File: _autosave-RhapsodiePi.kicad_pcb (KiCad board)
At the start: 6 copper layers, 85.2 x 56.1 mm, 261 parts, among them J1 Micro_SD_Card_Det, J2 Conn_Coaxial, J3 Conn_02x05_Odd_Even, J4 USB_A_Stacked, J5 USB_A_Stacked, J7 RJ45_HR913550A, J8 HDMI_A, J9 AudioJack4, P1 USB_C_Plug, U1 IMX6UL, U10 FE2.1, U11 RTL8201F, U12 TFP410PAP, U13 LM4871, U14 LM4871, U15 TPS65185RGZR, U2 MT3420C-mt3420c, U3 MT3420C-mt3420c, U4 MT3420C-mt3420c, U5 MKDN0xxxCL, U6 MT41K256M16TW, U7 MT41K256M16TW, U8 X1000, U9 AP6212, Y1 12MHz, Y2 24MHz, Y3 32.768kHz

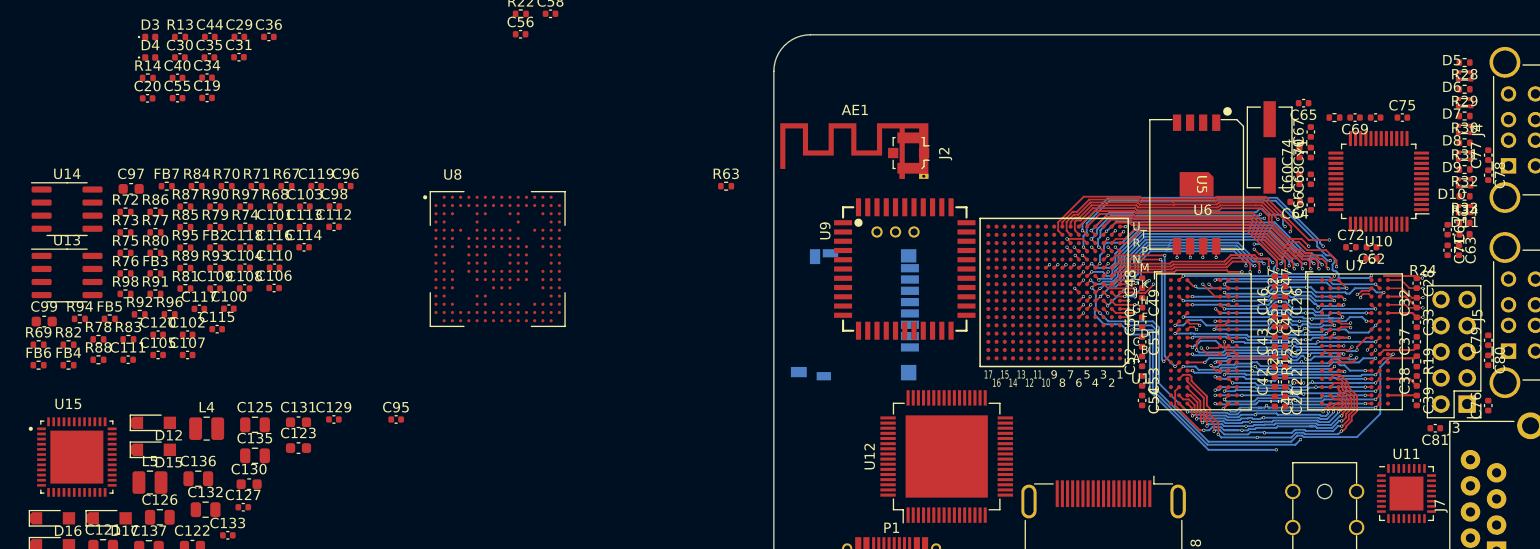
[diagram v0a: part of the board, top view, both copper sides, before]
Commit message: update DDR
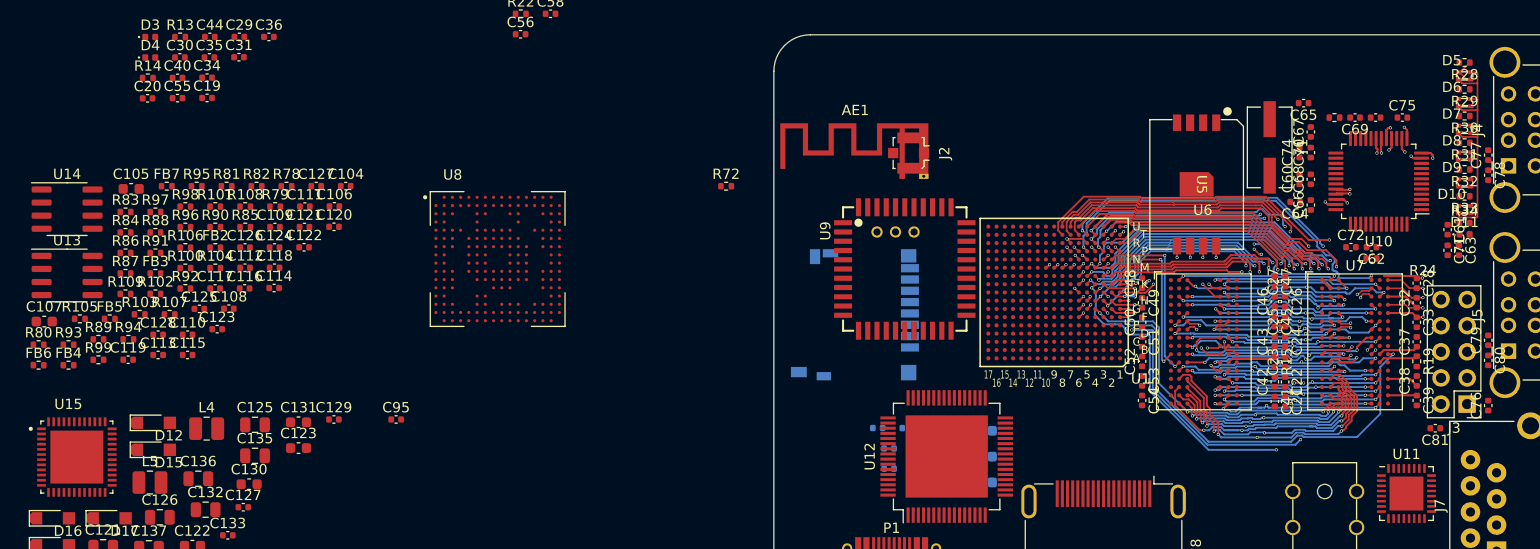
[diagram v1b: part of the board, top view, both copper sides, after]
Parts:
- added C100: 22µ, Capacitor_SMD:C_0603_1608Metric, B.Cu at (104.8, 107.9)
- added C101: 100n, Capacitor_SMD:C_0402_1005Metric, B.Cu at (95.5, 106.5)
- added C102: 100n, Capacitor_SMD:C_0402_1005Metric, B.Cu at (94.4, 102.6)
- added C103: 100n, Capacitor_SMD:C_0402_1005Metric, B.Cu at (98.4, 107.1)
- added C96: 22µ, Capacitor_SMD:C_0603_1608Metric, B.Cu at (104.8, 102.8)
- added C97: 100n, Capacitor_SMD:C_0402_1005Metric, B.Cu at (95.5, 104.6)
- added C98: 22µ, Capacitor_SMD:C_0603_1608Metric, B.Cu at (104.8, 105.4)
- added C99: 22µ, Capacitor_SMD:C_0603_1608Metric, B.Cu at (100.8, 102.8)
- added R62: 330, Resistor_SMD:R_0402_1005Metric, B.Cu at (97.3, 102.6)
- added R63: 330, Resistor_SMD:R_0402_1005Metric, B.Cu at (101.3, 105.1)
- added R67: 330, Resistor_SMD:R_0402_1005Metric, B.Cu at (98.4, 105.1)
- added R71: 2K7, Resistor_SMD:R_0402_1005Metric, B.Cu at (101.3, 107.1)
- renumbered C96 to C104, C97 to C105, C98 to C106, C99 to C107, C100 to C108, C101 to C109, C102 to C110, C103 to C111, C104 to C112, C105 to C113, C106 to C114, C107 to C115, C108 to C116, C109 to C117, C110 to C118, C111 to C119, C112 to C120, C113 to C121, C114 to C122, C115 to C123, C116 to C124, C117 to C125, C118 to C126, C119 to C127, C120 to C128, R89 to R100, R90 to R101, R91 to R102, R92 to R103, R93 to R104, R94 to R105, R95 to R106, R96 to R107, R97 to R108, R98 to R109, R63 to R72, R67 to R78, R68 to R79, R69 to R80, R70 to R81, R71 to R82, R72 to R83, R73 to R84, R74 to R85, R75 to R86, R76 to R87, R77 to R88, R78 to R89, R79 to R90, R80 to R91, R81 to R92, R82 to R93, R83 to R94, R84 to R95, R85 to R96, R86 to R97, R87 to R98, R88 to R99
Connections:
- net Net-(J4-Pad2) renamed /USB/D1-
- net Net-(J4-Pad3) renamed /USB/D1+
- net Net-(J4-Pad6) renamed /USB/D2-
- net Net-(J4-Pad7) renamed /USB/D2+
- net Net-(J5-Pad2) renamed /USB/D3-
- net Net-(J5-Pad3) renamed /USB/D3+
- net Net-(J5-Pad6) renamed /USB/D4-
- net Net-(J5-Pad7) renamed /USB/D4+
- AE1 pad 2: AGND2 -> GND
- C1 pad 2: AGND2 -> GND
- C10 pad 1: AGND2 -> GND
- C104 pad 1: AGND2 -> GND
- C105 pad 1: AGND2 -> GND
- C106 pad 1: AGND2 -> GND
- C107 pad 1: AGND2 -> GND
- C108 pad 2: AGND2 -> GND
- C11 pad 2: AGND2 -> GND
- C119 pad 1: AGND2 -> GND
- C12 pad 1: AGND2 -> GND
- C121 pad 2: AGND2 -> GND
- C122 pad 1: AGND2 -> GND
- C124 pad 2: AGND2 -> GND
- C125 pad 1: AGND2 -> GND
- C126 pad 1: AGND2 -> GND
- C127 pad 1: Net-(C119-Pad1) -> Net-(C127-Pad1)
- C127 pad 2: AGND2 -> GND
- C128 pad 1: Net-(C120-Pad1) -> Net-(C128-Pad1)
- C128 pad 2: AGND2 -> GND
- C13 pad 2: AGND2 -> GND
- C14 pad 1: AGND2 -> GND
- C15 pad 1: AGND2 -> GND
- C16 pad 1: AGND2 -> GND
- C17 pad 2: AGND2 -> GND
- C18 pad 1: AGND2 -> GND
- C19 pad 2: AGND2 -> GND
- C2 pad 2: AGND2 -> GND
- C20 pad 2: AGND2 -> GND
- C21 pad 2: AGND2 -> GND
- C22 pad 2: AGND2 -> GND
- C23 pad 2: AGND2 -> GND
- C24 pad 2: AGND2 -> GND
- C25 pad 2: AGND2 -> GND
- C26 pad 2: AGND2 -> GND
- C27 pad 2: AGND2 -> GND
- C28 pad 2: AGND2 -> GND
- C29 pad 2: AGND2 -> GND
- C3 pad 2: AGND2 -> GND
- C30 pad 2: AGND2 -> GND
- C31 pad 2: AGND2 -> GND
- C32 pad 2: AGND2 -> GND
- C33 pad 2: AGND2 -> GND
- C34 pad 2: AGND2 -> GND
- C35 pad 2: AGND2 -> GND
- C36 pad 2: AGND2 -> GND
- C37 pad 2: AGND2 -> GND
- C38 pad 2: AGND2 -> GND
- C39 pad 2: AGND2 -> GND
- C4 pad 2: AGND2 -> GND
- C40 pad 2: AGND2 -> GND
- C41 pad 2: AGND2 -> GND
- C42 pad 2: AGND2 -> GND
- C43 pad 2: AGND2 -> GND
- C44 pad 2: AGND2 -> GND
- C45 pad 2: AGND2 -> GND
- C46 pad 2: AGND2 -> GND
- C47 pad 2: AGND2 -> GND
- C48 pad 2: AGND2 -> GND
- C49 pad 2: AGND2 -> GND
- C5 pad 2: AGND2 -> GND
- C50 pad 2: AGND2 -> GND
- C51 pad 2: AGND2 -> GND
- C52 pad 2: AGND2 -> GND
- C53 pad 2: AGND2 -> GND
- C54 pad 2: AGND2 -> GND
- C55 pad 2: AGND2 -> GND
- C56 pad 2: AGND2 -> GND
- C57 pad 2: AGND2 -> GND
- C58 pad 2: AGND2 -> GND
- C59 pad 2: AGND2 -> GND
- C6 pad 2: AGND2 -> GND
- C60 pad 2: AGND2 -> GND
- C61 pad 2: AGND2 -> GND
- C62 pad 2: AGND2 -> GND
- C63 pad 2: AGND2 -> GND
- C64 pad 1: AGND2 -> GND
- C65 pad 1: AGND2 -> GND
- C66 pad 2: AGND2 -> GND
- C67 pad 2: AGND2 -> GND
- C68 pad 2: AGND2 -> GND
- C69 pad 2: AGND2 -> GND
- C7 pad 2: AGND2 -> GND
- C70 pad 2: AGND2 -> GND
- C71 pad 2: AGND2 -> GND
- C72 pad 1: AGND2 -> GND
- C73 pad 2: AGND2 -> GND
- C74 pad 2: AGND2 -> GND
- C75 pad 2: AGND2 -> GND
- C76 pad 2: AGND2 -> GND
- C77 pad 2: AGND2 -> GND
- C78 pad 2: AGND2 -> GND
- C79 pad 2: AGND2 -> GND
- C8 pad 2: AGND2 -> GND
- C80 pad 2: AGND2 -> GND
- C81 pad 2: AGND2 -> GND
- C82 pad 1: AGND2 -> GND
- C83 pad 1: AGND2 -> GND
- C84 pad 1: AGND2 -> GND
- C85 pad 1: AGND2 -> GND
- C86 pad 1: AGND2 -> GND
- C87 pad 2: AGND2 -> GND
- C88 pad 2: AGND2 -> GND
- C89 pad 1: AGND2 -> GND
- C9 pad 1: AGND2 -> GND
- C90 pad 1: AGND2 -> GND
- C91 pad 1: AGND2 -> GND
- C92 pad 1: AGND2 -> GND
- C93 pad 1: AGND2 -> GND
- C94 pad 1: AGND2 -> GND
- C95 pad 2: AGND2 -> GND
- D11 pad 1: AGND2 -> GND
- D3 pad 1: AGND2 -> GND
- D4 pad 1: AGND2 -> GND
- J1 pad 10: AGND2 -> GND
- J1 pad 6: AGND2 -> GND
- J2 pad 2: AGND2 -> GND
- J3 pad 7: AGND2 -> GND
- J3 pad 8: AGND2 -> GND
- J4 pad 4: AGND2 -> GND
- J4 pad 8: AGND2 -> GND
- J4 pad 9: AGND2 -> GND
- J5 pad 4: AGND2 -> GND
- J5 pad 8: AGND2 -> GND
- J5 pad 9: AGND2 -> GND
- J7 pad 8: AGND2 -> GND
- J7 pad SH: AGND2 -> GND
- J8 pad 11: AGND2 -> GND
- J8 pad 14: unconnected-(J8-Pad14) -> Net-(J8-Pad14)
- J8 pad 17: AGND2 -> GND
- J8 pad 2: AGND2 -> GND
- J8 pad 5: AGND2 -> GND
- J8 pad 8: AGND2 -> GND
- J8 pad SH: AGND2 -> GND
- P1 pad A1: AGND2 -> GND
- P1 pad A12: AGND2 -> GND
- P1 pad B1: AGND2 -> GND
- P1 pad B12: AGND2 -> GND
- P1 pad S1: AGND2 -> GND
- R101 pad 2: Net-(C119-Pad1) -> Net-(C127-Pad1)
- R103 pad 2: Net-(C120-Pad1) -> Net-(C128-Pad1)
- R15 pad 2: AGND2 -> GND
- R19 pad 2: AGND2 -> GND
- R26 pad 1: AGND2 -> GND
- R27 pad 2: AGND2 -> GND
- R38 pad 2: AGND2 -> GND
- R4 pad 2: AGND2 -> GND
- R40 pad 2: AGND2 -> GND
- R42 pad 2: AGND2 -> GND
- R44 pad 1: AGND2 -> GND
- R6 pad 2: AGND2 -> GND
- R79 pad 2: AGND2 -> GND
- R8 pad 2: AGND2 -> GND
- U1 pad A1: AGND2 -> GND
- U1 pad A17: AGND2 -> GND
- U1 pad C11: AGND2 -> GND
- U1 pad C15: AGND2 -> GND
- U1 pad C3: AGND2 -> GND
- U1 pad C7: AGND2 -> GND
- U1 pad E11: AGND2 -> GND
- U1 pad E13: unconnected-(U1-PadE13) -> Net-(C96-Pad2)
- U1 pad E8: AGND2 -> GND
- U1 pad F10: AGND2 -> GND
- U1 pad F11: AGND2 -> GND
- U1 pad F12: AGND2 -> GND
- U1 pad F6: AGND2 -> GND
- U1 pad F7: AGND2 -> GND
- U1 pad F8: AGND2 -> GND
- U1 pad F9: AGND2 -> GND
- U1 pad G12: AGND2 -> GND
- U1 pad G15: AGND2 -> GND
- U1 pad G3: AGND2 -> GND
- U1 pad G5: AGND2 -> GND
- U1 pad G7: AGND2 -> GND
- U1 pad H12: AGND2 -> GND
- U1 pad H7: AGND2 -> GND
- U1 pad J12: AGND2 -> GND
- U1 pad J5: AGND2 -> GND
- U1 pad J7: AGND2 -> GND
- U1 pad K12: AGND2 -> GND
- U1 pad K7: AGND2 -> GND
- U1 pad L12: AGND2 -> GND
- U1 pad L3: AGND2 -> GND
- U1 pad L7: AGND2 -> GND
- U1 pad M10: AGND2 -> GND
- U1 pad M11: AGND2 -> GND
- U1 pad M12: AGND2 -> GND
- U1 pad M7: AGND2 -> GND
- U1 pad M8: AGND2 -> GND
- U1 pad M9: AGND2 -> GND
- U1 pad N3: AGND2 -> GND
- U1 pad N5: AGND2 -> GND
- U1 pad R11: AGND2 -> GND
- U1 pad R16: AGND2 -> GND
- U1 pad R17: AGND2 -> GND
- U1 pad R3: AGND2 -> GND
- U1 pad R5: AGND2 -> GND
- U1 pad R7: AGND2 -> GND
- U1 pad T14: AGND2 -> GND
- U1 pad U1: AGND2 -> GND
- U1 pad U14: AGND2 -> GND
- U1 pad U17: AGND2 -> GND
- U10 pad 10: AGND2 -> GND
- U10 pad 24: AGND2 -> GND
- U10 pad 39: AGND2 -> GND
- U11 pad 33: AGND2 -> GND
- U12 pad 1: +3V3 -> Net-(C102-Pad1)
- U12 pad 10: unconnected-(U12-Pad10) -> Net-(R70-Pad2)
- U12 pad 11: unconnected-(U12-Pad11) -> Net-(R69-Pad2)
- U12 pad 12: +3V3 -> Net-(C102-Pad1)
- U12 pad 14: unconnected-(U12-Pad14) -> Net-(R67-Pad2)
- U12 pad 15: unconnected-(U12-Pad15) -> Net-(R71-Pad2)
- U12 pad 16: AGND2 -> GND
- U12 pad 17: AGND2 -> GND
- U12 pad 18: +3V3 -> Net-(C101-Pad1)
- U12 pad 20: AGND2 -> GND
- U12 pad 23: +3V3 -> Net-(C100-Pad1)
- U12 pad 26: AGND2 -> GND
- U12 pad 29: +3V3 -> Net-(C100-Pad1)
- U12 pad 32: AGND2 -> GND
- U12 pad 33: +3V3 -> Net-(C102-Pad1)
- U12 pad 34: unconnected-(U12-Pad34) -> Net-(R73-Pad1)
- U12 pad 35: unconnected-(U12-Pad35) -> Net-(R63-Pad1)
- U12 pad 48: AGND2 -> GND
- U12 pad 6: unconnected-(U12-Pad6) -> Net-(R66-Pad1)
- U12 pad 64: AGND2 -> GND
- U12 pad 65: AGND2 -> GND
- U12 pad 7: unconnected-(U12-Pad7) -> Net-(R65-Pad1)
- U12 pad 8: unconnected-(U12-Pad8) -> Net-(R64-Pad1)
- U12 pad 9: unconnected-(U12-Pad9) -> Net-(R62-Pad1)
- U13 pad 2: Net-(C119-Pad1) -> Net-(C127-Pad1)
- U13 pad 7: AGND2 -> GND
- U14 pad 2: Net-(C120-Pad1) -> Net-(C128-Pad1)
- U14 pad 7: AGND2 -> GND
- U2 pad 2: AGND2 -> GND
- U3 pad 2: AGND2 -> GND
- U4 pad 2: AGND2 -> GND
- U5 pad 4: AGND2 -> GND
- U6 pad A9: AGND2 -> GND
- U6 pad B1: AGND2 -> GND
- U6 pad B3: AGND2 -> GND
- U6 pad B9: AGND2 -> GND
- U6 pad D1: AGND2 -> GND
- U6 pad D8: AGND2 -> GND
- U6 pad E1: AGND2 -> GND
- U6 pad E2: AGND2 -> GND
- U6 pad E8: AGND2 -> GND
- U6 pad F9: AGND2 -> GND
- U6 pad G1: AGND2 -> GND
- U6 pad G8: AGND2 -> GND
- U6 pad G9: AGND2 -> GND
- U6 pad J2: AGND2 -> GND
- U6 pad J8: AGND2 -> GND
- U6 pad M1: AGND2 -> GND
- U6 pad M9: AGND2 -> GND
- U6 pad P1: AGND2 -> GND
- U6 pad P9: AGND2 -> GND
- U6 pad T1: AGND2 -> GND
- U6 pad T9: AGND2 -> GND
- U7 pad A9: AGND2 -> GND
- U7 pad B1: AGND2 -> GND
- U7 pad B3: AGND2 -> GND
- U7 pad B9: AGND2 -> GND
- U7 pad D1: AGND2 -> GND
- U7 pad D8: AGND2 -> GND
- U7 pad E1: AGND2 -> GND
- U7 pad E2: AGND2 -> GND
- U7 pad E8: AGND2 -> GND
- U7 pad F9: AGND2 -> GND
- U7 pad G1: AGND2 -> GND
- U7 pad G8: AGND2 -> GND
- U7 pad G9: AGND2 -> GND
- U7 pad J2: AGND2 -> GND
- U7 pad J8: AGND2 -> GND
- U7 pad M1: AGND2 -> GND
- U7 pad M9: AGND2 -> GND
- U7 pad P1: AGND2 -> GND
- U7 pad P9: AGND2 -> GND
- U7 pad T1: AGND2 -> GND
- U7 pad T9: AGND2 -> GND
- U9 pad 1: AGND2 -> GND
- U9 pad 20: AGND2 -> GND
- U9 pad 3: AGND2 -> GND
- U9 pad 31: AGND2 -> GND
- U9 pad 33: AGND2 -> GND
- U9 pad 36: AGND2 -> GND
- Y2 pad 1: AGND2 -> GND
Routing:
- net /USB/D4-: track 0.00 -> 35.6 mm, vias 0 -> 1
- net /USB/D4+: track 0.00 -> 32.7 mm, vias 0 -> 1
- net DP5-: track 0.00 -> 28.7 mm, vias 0 -> 1
- net /USB/D3-: track 0.00 -> 27.6 mm, vias 0 -> 1
- net DP5+: track 0.00 -> 27.5 mm, vias 0 -> 1
- net /USB/D2-: track 0.00 -> 26.0 mm, vias 0 -> 1
- net DP6+: track 0.00 -> 25.2 mm, vias 0 -> 1
- net DRV: track 0.00 -> 24.8 mm
- net /USB/D3+: track 0.00 -> 24.7 mm, vias 0 -> 1
- net /USB/D2+: track 0.00 -> 24.4 mm, vias 0 -> 1
- net DP6-: track 0.00 -> 23.0 mm, vias 0 -> 1
- net /USB/D1+: track 0.00 -> 19.6 mm, vias 0 -> 1
- net /USB/D1-: track 0.00 -> 19.0 mm, vias 0 -> 1
- net GND: track 0.00 -> 16.9 mm, vias 0 -> 15
- net AGND2: track 16.9 -> 0.00 mm, vias 15 -> 0
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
